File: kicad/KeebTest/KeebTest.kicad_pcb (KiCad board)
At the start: 2 copper layers, 104.8 x 69.1 mm, 19 parts, among them U1 Arduino_Pro_Micro

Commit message: update size
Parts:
- moved U1 15.7 mm to (175.5, 69.5)
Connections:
- U1 pad 10: ROW2 -> ROW0
- U1 pad 11: unconnected-(U1-8/PB4-Pad11) -> ROW1
- U1 pad 12: unconnected-(U1-9/PB5-Pad12) -> ROW2
- U1 pad 5: COL0 -> unconnected-(U1-2/PD1-Pad5)
- U1 pad 6: COL1 -> unconnected-(U1-3/PD0-Pad6)
- U1 pad 7: COL2 -> COL0
- U1 pad 8: ROW0 -> COL1
- U1 pad 9: ROW1 -> COL2
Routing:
- net ROW1: track 68.9 -> 49.8 mm
- net COL2: track 85.3 -> 67.1 mm
- net ROW2: track 78.6 -> 61.3 mm
- net COL0: track 124.8 -> 108.4 mm, vias 0 -> 2
- net COL1: track 106.7 -> 95.5 mm, vias 0 -> 2
- net ROW0: track 64.6 -> 57.3 mm
- added copper zone on B.Cu, net (none)
- added copper zone on F.Cu, net (none)
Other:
- board size 104.8 x 69.1 mm -> 88.1 x 61.9 mm

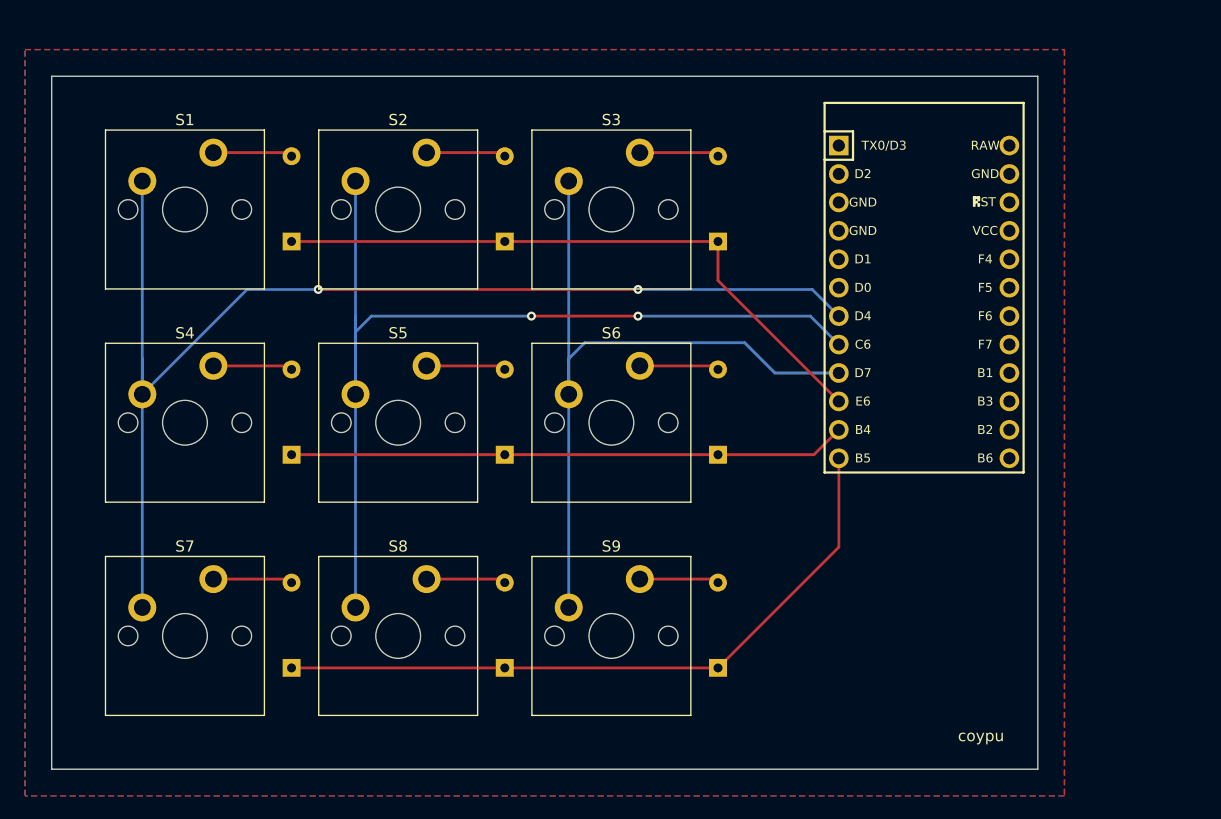
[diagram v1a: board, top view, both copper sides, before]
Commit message: update size
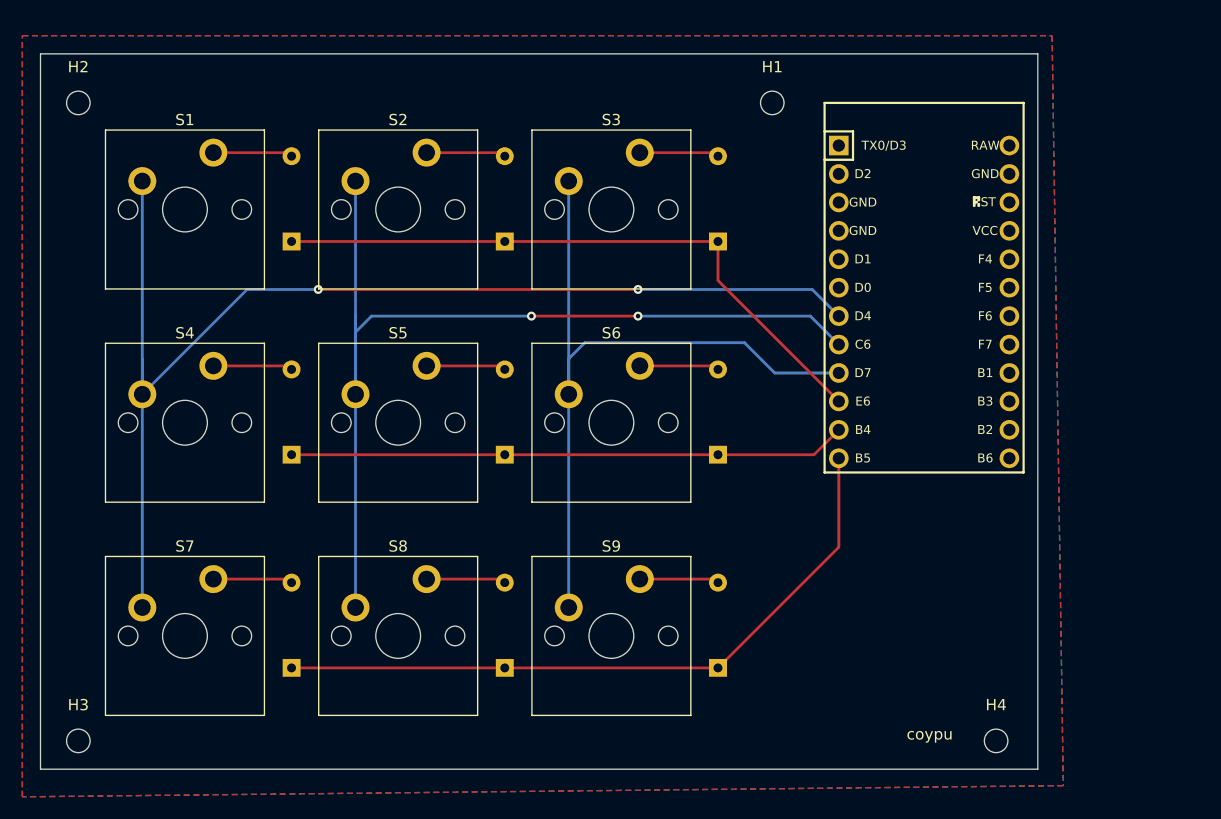
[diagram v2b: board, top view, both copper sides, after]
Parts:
- added H1: MountingHole, MountingHole:MountingHole_2.1mm, F.Cu at (161.9, 51.7)
- added H2: MountingHole, MountingHole:MountingHole_2.1mm, F.Cu at (99.9, 51.7)
- added H3: MountingHole, MountingHole:MountingHole_2.1mm, F.Cu at (99.9, 108.7)
- added H4: MountingHole, MountingHole:MountingHole_2.1mm, F.Cu at (181.9, 108.7)
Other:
- board size 88.1 x 61.9 mm -> 89.1 x 63.9 mm
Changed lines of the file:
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@@
     )
+  )
+  (footprint "MountingHole:MountingHole_2.1mm" (layer "F.Cu")
+    (at 99.949 108.689)
+    (descr "Mounting Hole 2.1mm, no annular")
+    (tags "mounting hole 2.1mm no annular")
+    (property "Sheetfile" "KeebTest.kicad_sch")
+    (property "Sheetname" "")
+    (property "ki_description" "Mounting Hole without connection")
+    (property "ki_keywords" "mounting hole")
+    (attr exclude_from_pos_files)
+    (fp_text reference "H3" (at 0 -3.2) (layer "F.SilkS")
+        (effects (font (size 1 1) (thickness 0.15)))
+    )
+    (fp_text value "MountingHole" (at 0 3.2) (layer "F.Fab")
+        (effects (font (size 1 1) (thickness 0.15)))
+    )
+    (fp_circle (center 0 0) (end 2.1 0)
+      (stroke (width 0.15) (type solid)) (fill none) (layer "Cmts.User"))
+    (fp_circle (center 0 0) (end 2.35 0)
+      (stroke (width 0.05) (type solid)) (fill none) (layer "F.CrtYd"))
+    (pad "" np_thru_hole circle (at 0 0) (size 2.1 2.1) (drill 2.1) (layers "*.Cu" "*.Mask"))
   )
   (footprint "ScottoKeebs_MX:MX_PCB_1.00u" (layer "F.Cu")
@@
     )
   )
+  (footprint "MountingHole:MountingHole_2.1mm" (layer "F.Cu")
+    (at 99.949 51.689)
+    (descr "Mounting Hole 2.1mm, no annular")
+    (tags "mounting hole 2.1mm no annular")
+    (property "Sheetfile" "KeebTest.kicad_sch")
+    (property "Sheetname" "")
+    (property "ki_description" "Mounting Hole without connection")
+    (property "ki_keywords" "mounting hole")
+    (attr exclude_from_pos_files)
+    (fp_text reference "H2" (at 0 -3.2) (layer "F.SilkS")
+        (effects (font (size 1 1) (thickness 0.15)))
+    )
+    (fp_text value "MountingHole" (at 0 3.2) (layer "F.Fab")
+        (effects (font (size 1 1) (thickness 0.15)))
+    )
+    (fp_text user "${REFERENCE}" (at 0 0) (layer "F.Fab")
+        (effects (font (size 1 1) (thickness 0.15)))
+    )
+    (fp_circle (center 0 0) (end 2.1 0)
+      (stroke (width 0.15) (type solid)) (fill none) (layer "Cmts.User"))
+    (fp_circle (center 0 0) (end 2.35 0)
+      (stroke (width 0.05) (type solid)) (fill none) (layer "F.CrtYd"))
+    (pad "" np_thru_hole circle (at 0 0) (size 2.1 2.1) (drill 2.1) (layers "*.Cu" "*.Mask"))
+  )
   (footprint "ScottoKeebs_MX:MX_PCB_1.00u" (layer "F.Cu")
     (at 147.574 99.314)
@@
       (rotate (xyz 0 0 0))
     )
+  )
+  (footprint "MountingHole:MountingHole_2.1mm" (layer "F.Cu")
+    (at 161.949 51.689)
+    (descr "Mounting Hole 2.1mm, no annular")
+    (tags "mounting hole 2.1mm no annular")
+    (property "Sheetfile" "KeebTest.kicad_sch")
+    (property "Sheetname" "")
+    (property "ki_description" "Mounting Hole without connection")
+    (property "ki_keywords" "mounting hole")
+    (attr exclude_from_pos_files)
+    (fp_text reference "H1" (at 0 -3.2) (layer "F.SilkS")
+        (effects (font (size 1 1) (thickness 0.15)))
+    )
+    (fp_text value "MountingHole" (at 0 3.2) (layer "F.Fab")
+        (effects (font (size 1 1) (thickness 0.15)))
+    )
+    (fp_text user "${REFERENCE}" (at 0 0) (layer "F.Fab")
+        (effects (font (size 1 1) (thickness 0.15)))
+    )
+    (fp_circle (center 0 0) (end 2.1 0)
+      (stroke (width 0.15) (type solid)) (fill none) (layer "Cmts.User"))
+    (fp_circle (center 0 0) (end 2.35 0)
+      (stroke (width 0.05) (type solid)) (fill none) (layer "F.CrtYd"))
+    (pad "" np_thru_hole circle (at 0 0) (size 2.1 2.1) (drill 2.1) (layers "*.Cu" "*.Mask"))
   )
   (footprint "ScottoKeebs_MCU:Arduino_Pro_Micro" (layer "F.Cu")
@@
     )
   )
+  (footprint "MountingHole:MountingHole_2.1mm" (layer "F.Cu")
+    (at 181.949 108.689)
+    (descr "Mounting Hole 2.1mm, no annular")
+    (tags "mounting hole 2.1mm no annular")
+    (property "Sheetfile" "KeebTest.kicad_sch")
+    (property "Sheetname" "")
+    (property "ki_description" "Mounting Hole without connection")
+    (property "ki_keywords" "mounting hole")
+    (attr exclude_from_pos_files)
+    (fp_text reference "H4" (at 0 -3.2) (layer "F.SilkS")
+        (effects (font (size 1 1) (thickness 0.15)))
+    )
+    (fp_text value "MountingHole" (at 0 3.2) (layer "F.Fab")
+        (effects (font (size 1 1) (thickness 0.15)))
+    )
+    (fp_text user "${REFERENCE}" (at 0 0) (layer "F.Fab")
+        (effects (font (size 1 1) (thickness 0.15)))
+    )
+    (fp_circle (center 0 0) (end 2.1 0)
+      (stroke (width 0.15) (type solid)) (fill none) (layer "Cmts.User"))
+    (fp_circle (center 0 0) (end 2.35 0)
+      (stroke (width 0.05) (type solid)) (fill none) (layer "F.CrtYd"))
+    (pad "" np_thru_hole circle (at 0 0) (size 2.1 2.1) (drill 2.1) (layers "*.Cu" "*.Mask"))
+  )
   (footprint "ScottoKeebs_MX:MX_PCB_1.00u" (layer "F.Cu")
     (at 128.524 99.314)
@@
     (property "ki_keywords" "diode")
     (attr through_hole)
-    (fp_text reference "D1" (at 3.81 2.12 -270) (layer "B.SilkS")
-        (effects (font (size 1 1) (thickness 0.15)) (justify mirror))
-    )
-    (fp_text value "Diode" (at 3.81 -2.12 -270) (layer "B.Fab")
-        (effects (font (size 1 1) (thickness 0.15)) (justify mirror))
-    )
-    (fp_text user "K" (at 0 1.8 -270) (layer "B.SilkS")
-        (effects (font (size 1 1) (thickness 0.15)) (justify mirror))
-    )
-    (fp_text user "${REFERENCE}" (at 4.11 0 -270) (layer "B.Fab")
+    (fp_text reference "D1" (at 3.81 2.12 270) (layer "B.SilkS")
+        (effects (font (size 1 1) (thickness 0.15)) (justify mirror))
+    )
+    (fp_text value "Diode" (at 3.81 -2.12 270) (layer "B.Fab")
+        (effects (font (size 1 1) (thickness 0.15)) (justify mirror))
+    )
+    (fp_text user "K" (at 0 1.8 270) (layer "B.SilkS")
+        (effects (font (size 1 1) (thickness 0.15)) (justify mirror))
+    )
+    (fp_text user "${REFERENCE}" (at 4.11 0 270) (layer "B.Fab")
         (effects (font (size 0.8 0.8) (thickness 0.12)) (justify mirror))
     )
-    (fp_text user "K" (at 0 1.8 -270) (layer "B.Fab")
+    (fp_text user "K" (at 0 1.8 270) (layer "B.Fab")
         (effects (font (size 1 1) (thickness 0.15)) (justify mirror))
     )
@@
     )
   )
-  (gr_rect (start 97.56775 49.30775) (end 185.674 111.22025)
+  (gr_circle (center 160.949 108.689) (end 160.949 108.689)
     (stroke (width 0.1) (type default)) (fill none) (layer "Edge.Cuts"))
-  (gr_text "coypu" (at 183.29275 108.839) (layer "B.SilkS")
+  (gr_rect (start 96.56775 47.30775) (end 185.674 111.22025)
+    (stroke (width 0.1) (type default)) (fill none) (layer "Edge.Cuts"))
+  (gr_text "coypu" (at 178.949 108.839) (layer "B.SilkS")
     (effects (font (size 1 1) (thickness 0.2) bold) (justify left bottom mirror))
   )
-  (gr_text "coypu" (at 178.53025 108.839) (layer "F.SilkS")
+  (gr_text "coypu" (at 173.949 108.689) (layer "F.SilkS")
     (effects (font (size 1 1) (thickness 0.15)) (justify left bottom))
   )
@@
     (polygon
       (pts
-        (xy 95.1865 46.9265)
-        (xy 188.05525 46.9265)
-        (xy 188.05525 113.6015)
-        (xy 95.1865 113.6015)
+        (xy 94.949 45.689)
+        (xy 186.949 45.689)
+        (xy 187.949 112.689)
+        (xy 94.949 113.689)
       )
     )
